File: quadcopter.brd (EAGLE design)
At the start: 137.2 x 137.2 mm, 69 parts, among them J4 AVR_SPI_PRG_6NS, M1 MOTOR_PADS, M2 MOTOR_PADS, M3 MOTOR_PADS, M4 MOTOR_PADS, U1 ATMEGA128RFA1

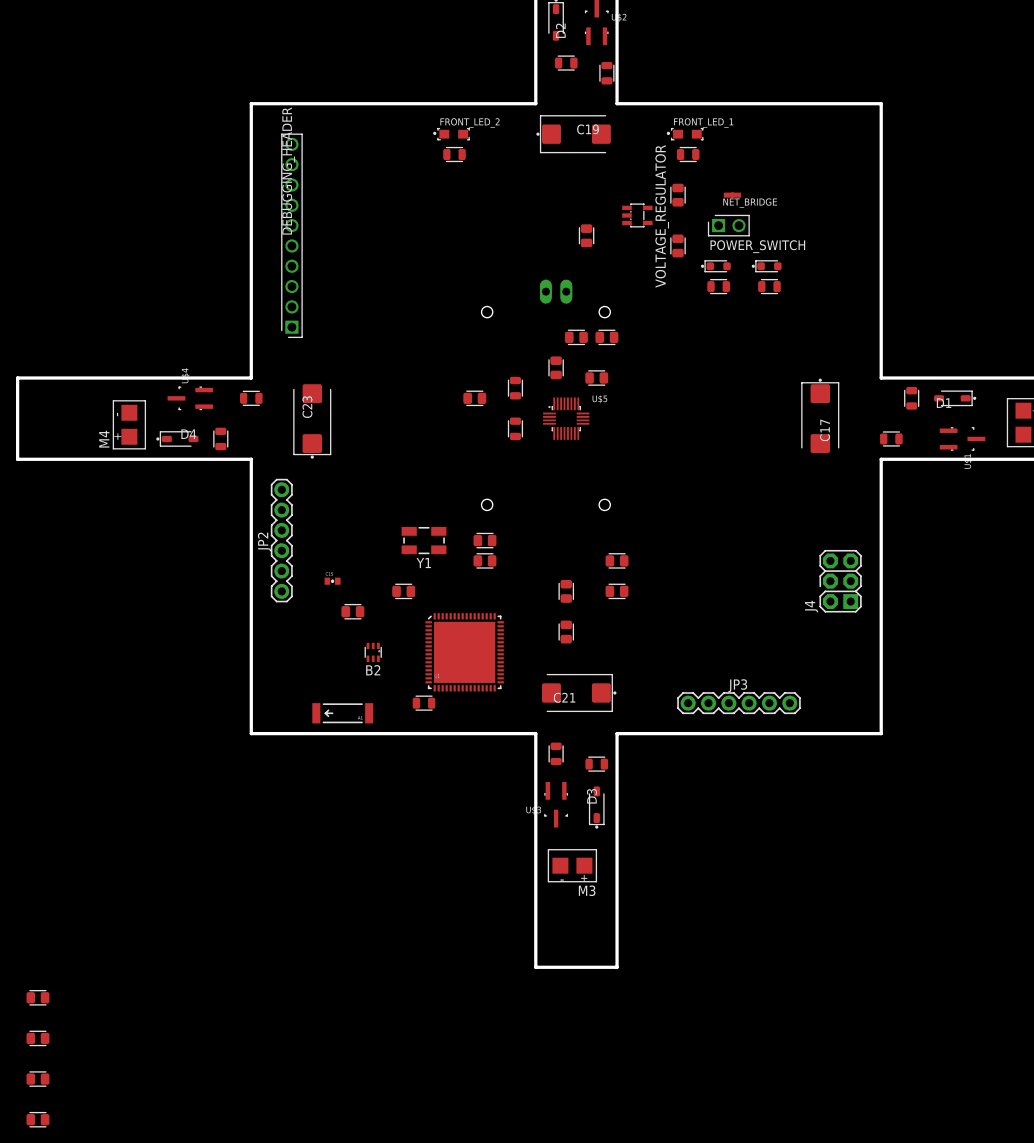
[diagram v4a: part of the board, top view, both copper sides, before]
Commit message: Finish Board Layers (still need to route
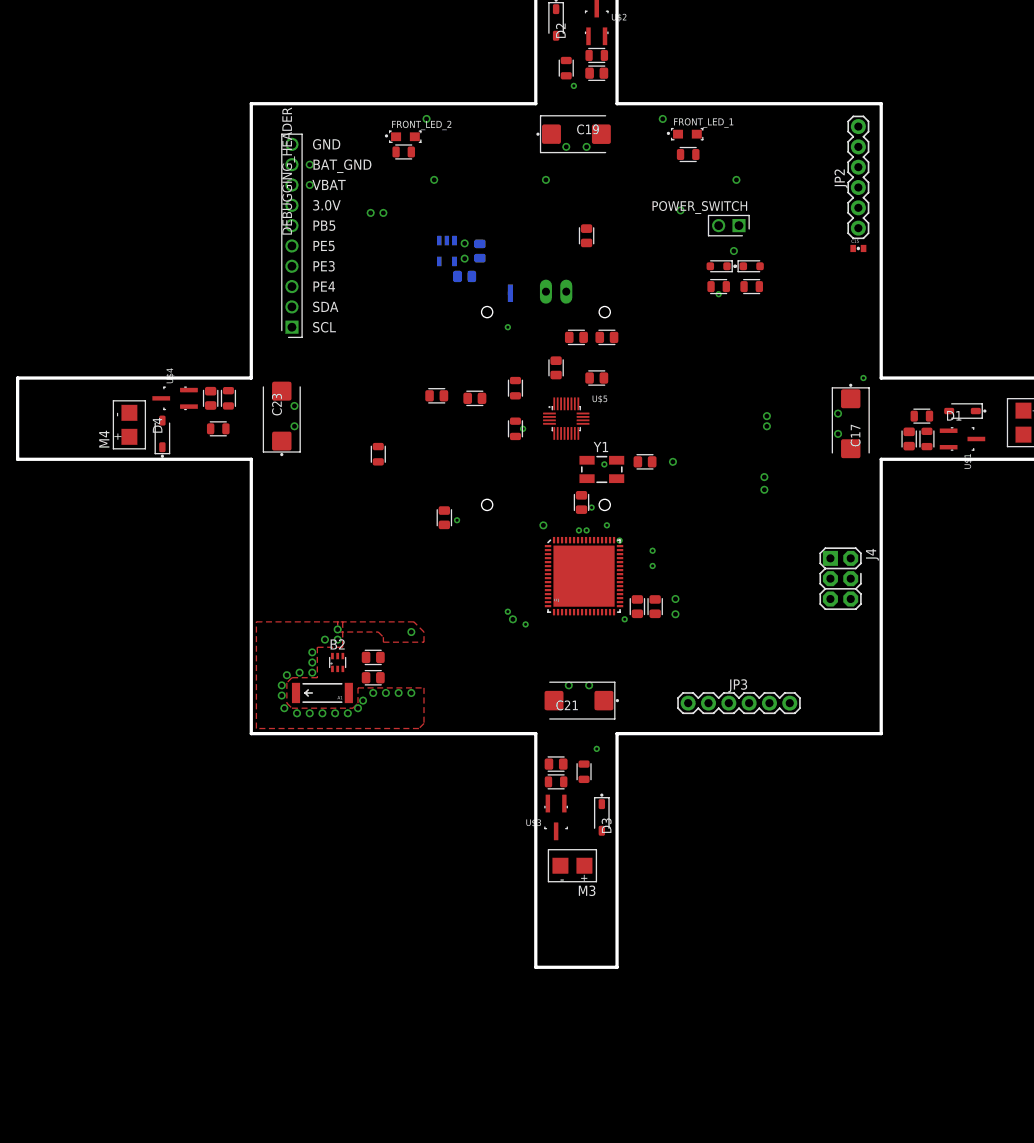
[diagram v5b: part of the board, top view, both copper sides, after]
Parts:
- moved C12 148.3 mm to (3.81, 43.2)
- moved C11 135.1 mm to (42.9, -2.54), turned to 270 degrees
- moved JP2 85.2 mm to (36.5, 23.8)
- moved C9 78.0 mm to (-44.5, 2.54), turned to 90 degrees
- moved C15 77.8 mm to (36.5, 21.3)
- moved C10 73.3 mm to (-1.27, -43.2), turned to 180 degrees
- moved C2 33.7 mm to (-16.2, 2.86), turned to 180 degrees
- moved R1 31.6 mm to (-23.5, -4.45), turned to 90 degrees
- moved NET_BRIDGE 30.1 mm to (-6.99, 15.2), flipped to the bottom, turned to 90 degrees
- moved C26 26.9 mm to (-12.7, 17.8), flipped to the bottom, turned to 180 degrees
- moved C25 25.7 mm to (-10.8, 21.0), flipped to the bottom, turned to 90 degrees
- moved VOLTAGE_REGULATOR 24.2 mm to (-14.9, 21.0), flipped to the bottom, turned to 180 degrees
- moved Y1 23.9 mm to (4.45, -6.35), turned to 0 degrees
- moved C4 23.5 mm to (9.84, -5.40)
- moved C1 17.8 mm to (-15.2, -12.4), turned to 270 degrees
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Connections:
- net FILTERED1: now also C9.1
- net FILTERED2: now also C12.1
- net FILTERED3: now also C10.1
- net FILTERED4: now also C11.1
- net GND: now also B2.5; no longer B2.1
- net PB5: no longer C9.1
- net PE3: no longer C10.1
- net PE4: no longer C11.1
- net PE5: no longer C12.1
- net RFANT: now also B2.1; no longer B2.5
- net RFN: now also B2.3; no longer B2.4
- net RFP: now also B2.4; no longer B2.3
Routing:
- added copper zone on layer 2, net 3.0V
- added copper zone on layer 1, net GND
- added copper zone on layer 15, net GND
- added copper zone on layer 2, net GND
- added copper zone on layer 2, net N$6
- added copper zone on layer 2, net VBAT
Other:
- board text added: "3.0V"
- board text added: "BAT_GND"
- board text added: "GND"
- board text added: "PB5"
- board text added: "PE3"
- board text added: "PE4"
- board text added: "PE5"
- board text added: "SCL"
- board text added: "SDA"
- board text added: "VBAT"

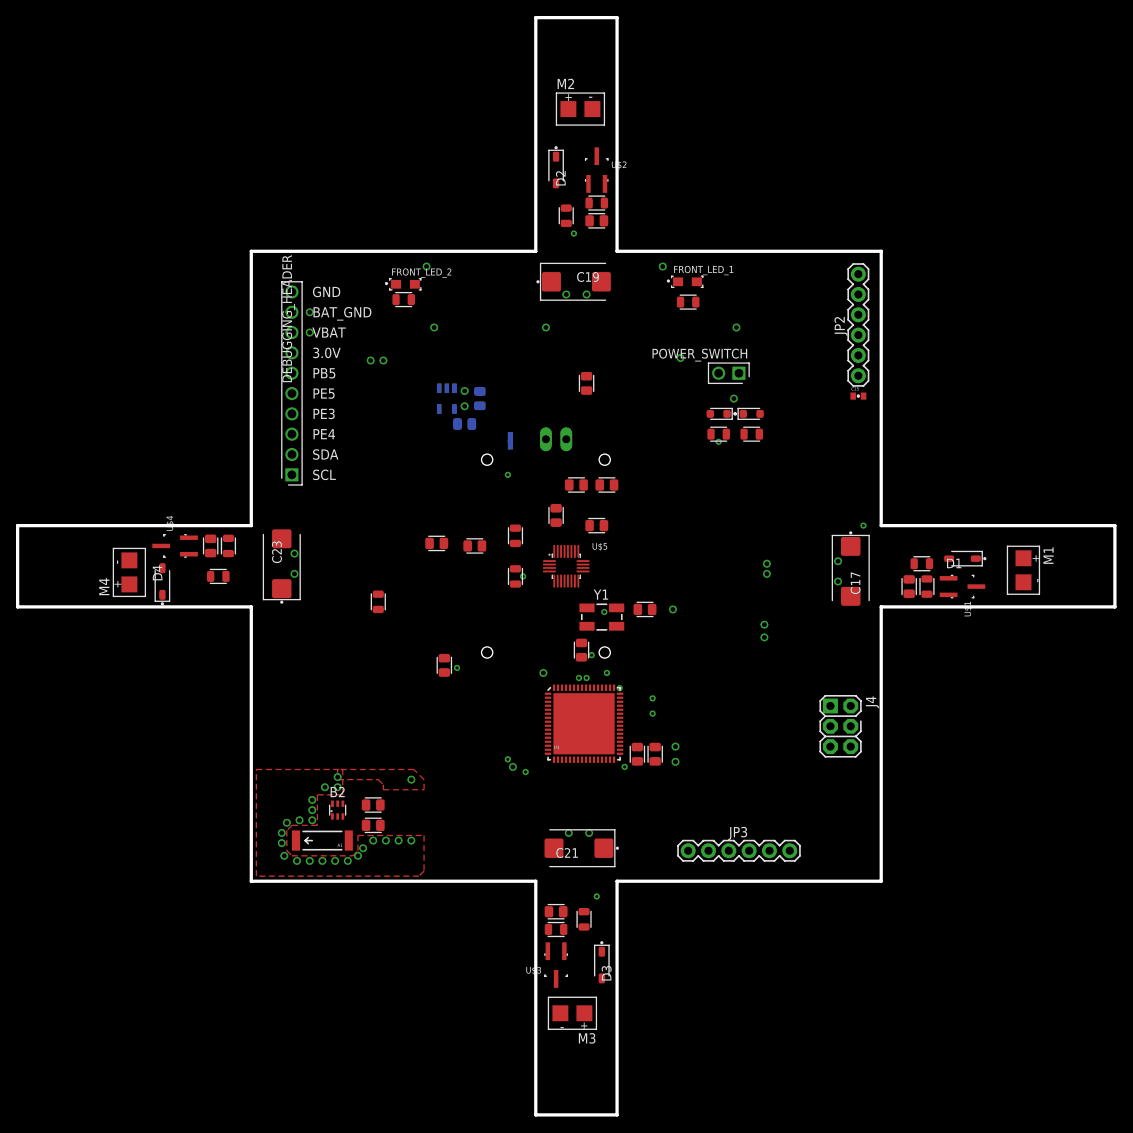
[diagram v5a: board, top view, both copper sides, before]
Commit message: Ran Autorouter but did not fix errros
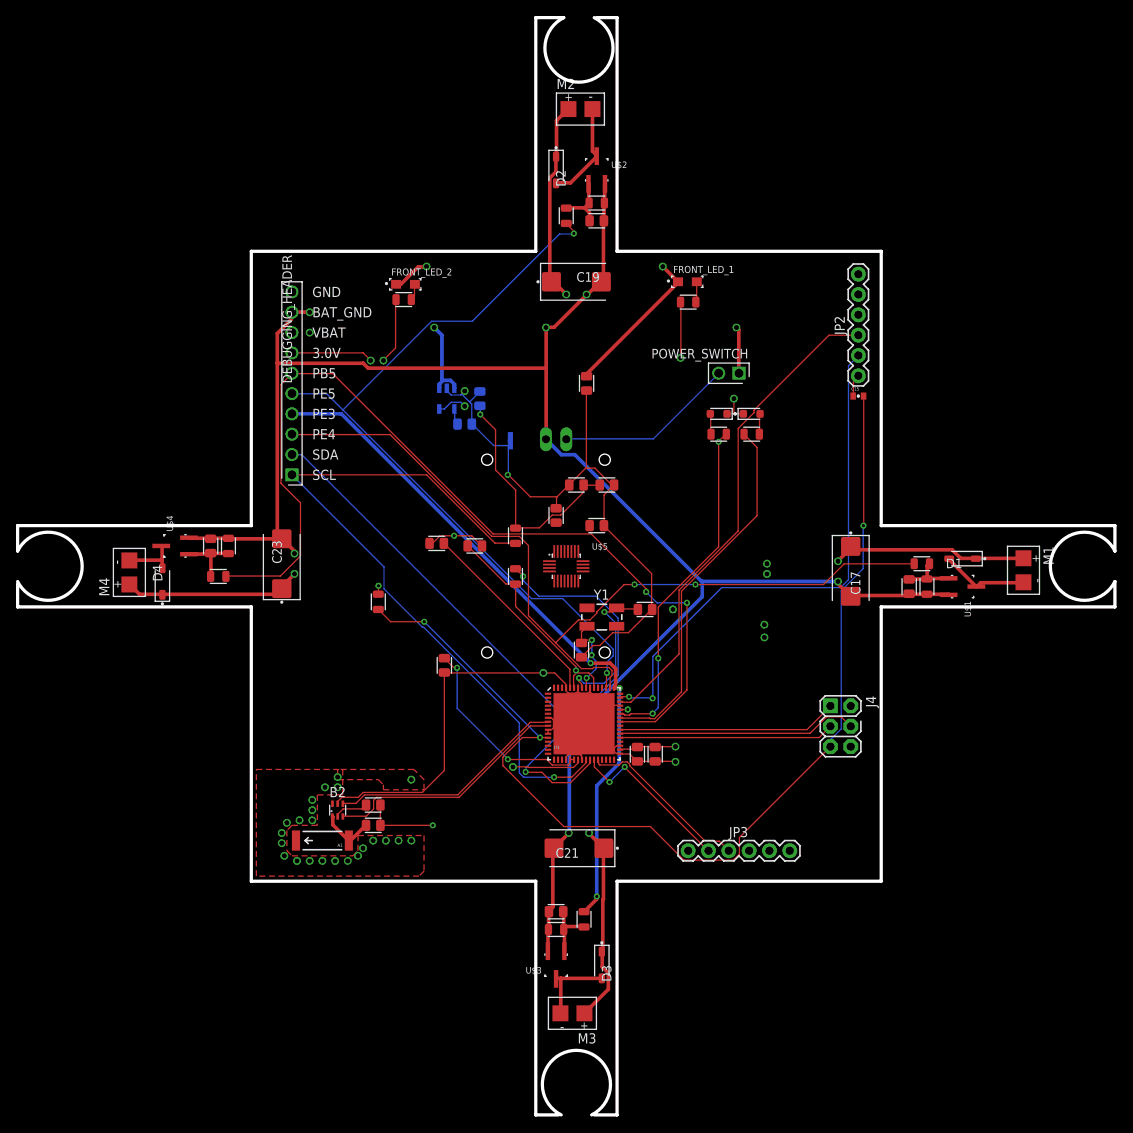
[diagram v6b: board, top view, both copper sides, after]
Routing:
- net GND: track 0.00 -> 232.9 mm, vias 32 -> 34
- net BAT_GND: track 0.00 -> 228.6 mm
- net VBAT: track 0.00 -> 137.7 mm
- net RESET: track 0.00 -> 133.1 mm, vias 1 -> 3
- net PB5: track 0.00 -> 117.2 mm, vias 0 -> 2
- net PE4: track 0.00 -> 108.8 mm, vias 0 -> 2
- net SDA: track 0.00 -> 98.5 mm
- net PE5: track 0.00 -> 98.4 mm
- net 3.0V: track 0.00 -> 90.4 mm, vias 7 -> 11
- net SCL: track 0.00 -> 90.3 mm, vias 0 -> 1
- net PE3: track 0.00 -> 86.6 mm, vias 2 -> 3
- net TX0: track 0.00 -> 66.4 mm, vias 1 -> 2
- net RX0: track 0.00 -> 61.2 mm
- net PB6: track 0.00 -> 45.9 mm
- net PB7: track 0.00 -> 43.0 mm, vias 2 -> 3
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- added copper zone on layer 15, net N$11
- added copper zone on layer 2, net N$9
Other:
- outline, holes or cut-outs redrawn
